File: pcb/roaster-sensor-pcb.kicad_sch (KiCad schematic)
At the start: 3 parts, among them U1 Pico

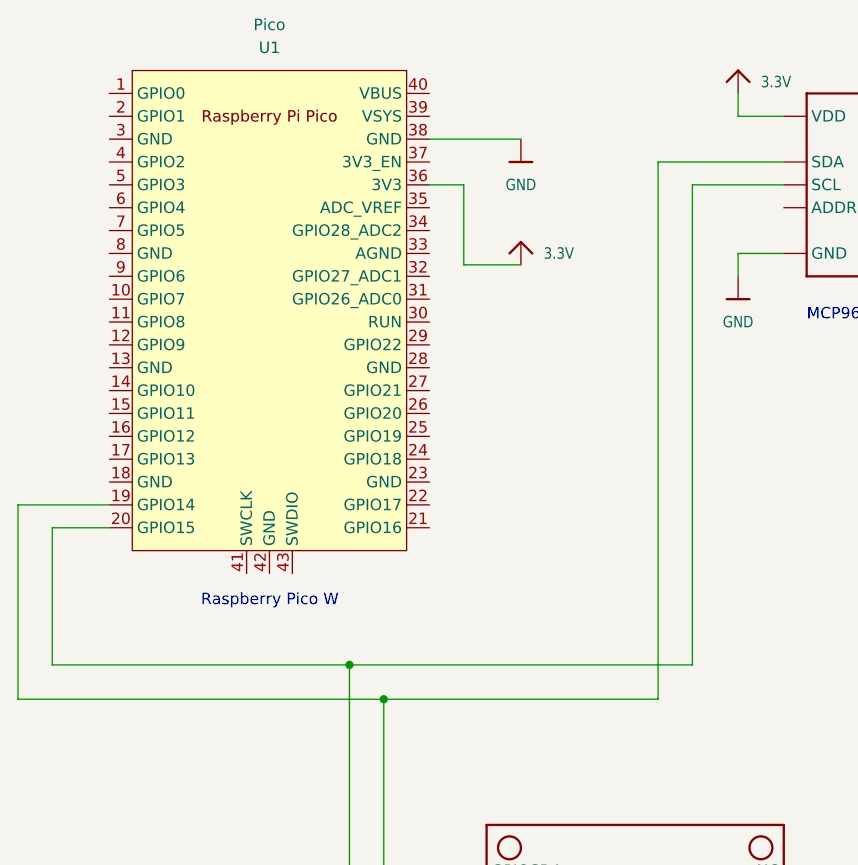
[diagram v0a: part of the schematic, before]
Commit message: changed pinout and disable display for perf proto
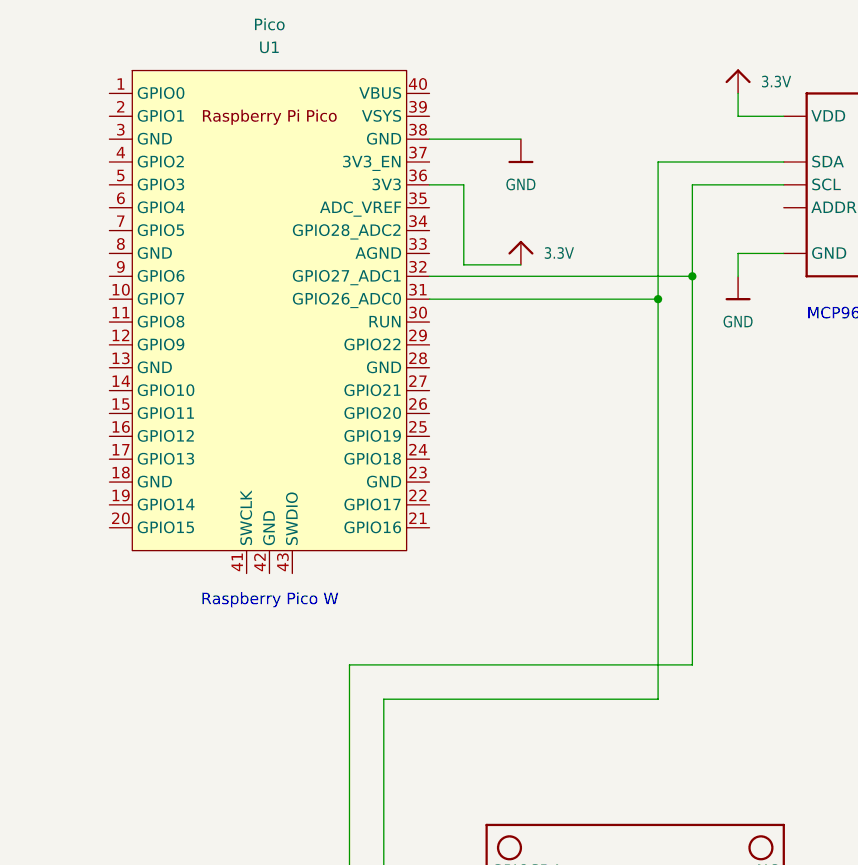
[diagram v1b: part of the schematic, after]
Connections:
- net at MS1.17 (GPIOSDA), MS1.17B (GPIOSDA), U2.20 (SDA): now also U1.31 (GPIO26_ADC0); no longer U1.19 (GPIO14)
- net at MS1.18 (GPIOSCL), MS1.18B (GPIOSCL), U2.19 (SCL): now also U1.32 (GPIO27_ADC1); no longer U1.20 (GPIO15)
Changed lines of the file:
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@@
 (kicad_sch (version 20230121) (generator eeschema)
   (paper "A4")
-  (junction (at 90.17 102.87) (diameter 0) (color 0 0 0 0)
-  )
-  (junction (at 86.36 99.06) (diameter 0) (color 0 0 0 0)
+  (junction (at 120.65 58.42) (diameter 0) (color 0 0 0 0)
   )
   (junction (at 148.59 157.48) (diameter 0) (color 0 0 0 0)
+  )
+  (junction (at 124.46 55.88) (diameter 0) (color 0 0 0 0)
   )
   (wire (pts (xy 90.17 102.87) (xy 120.65 102.87))
@@
   )
   (wire (pts (xy 90.17 121.92) (xy 96.52 121.92))
-    (stroke (width 0) (type default))
-  )
-  (wire (pts (xy 59.69 81.28) (xy 49.53 81.28))
     (stroke (width 0) (type default))
   )
@@
     (stroke (width 0) (type default))
   )
-  (wire (pts (xy 53.34 83.82) (xy 53.34 99.06))
-    (stroke (width 0) (type default))
-  )
   (wire (pts (xy 129.54 55.88) (xy 129.54 53.34))
     (stroke (width 0) (type default))
@@
     (stroke (width 0) (type default))
   )
-  (wire (pts (xy 49.53 102.87) (xy 90.17 102.87))
-    (stroke (width 0) (type default))
-  )
   (wire (pts (xy 95.25 40.64) (xy 105.41 40.64))
     (stroke (width 0) (type default))
   )
-  (wire (pts (xy 120.65 43.18) (xy 120.65 102.87))
+  (wire (pts (xy 120.65 43.18) (xy 120.65 58.42))
     (stroke (width 0) (type default))
   )
@@
     (stroke (width 0) (type default))
   )
-  (wire (pts (xy 124.46 99.06) (xy 124.46 45.72))
+  (wire (pts (xy 124.46 99.06) (xy 124.46 55.88))
     (stroke (width 0) (type default))
   )
@@
     (stroke (width 0) (type default))
   )
+  (wire (pts (xy 124.46 55.88) (xy 124.46 45.72))
+    (stroke (width 0) (type default))
+  )
   (wire (pts (xy 143.51 152.4) (xy 139.7 152.4))
     (stroke (width 0) (type default))
@@
     (stroke (width 0) (type default))
   )
-  (wire (pts (xy 59.69 83.82) (xy 53.34 83.82))
-    (stroke (width 0) (type default))
-  )
   (wire (pts (xy 139.7 157.48) (xy 148.59 157.48))
     (stroke (width 0) (type default))
@@
     (stroke (width 0) (type default))
   )
+  (wire (pts (xy 120.65 58.42) (xy 120.65 102.87))
+    (stroke (width 0) (type default))
+  )
   (wire (pts (xy 148.59 147.32) (xy 143.51 147.32))
     (stroke (width 0) (type default))
   )
-  (wire (pts (xy 49.53 81.28) (xy 49.53 102.87))
+  (wire (pts (xy 95.25 55.88) (xy 124.46 55.88))
     (stroke (width 0) (type default))
   )
-  (wire (pts (xy 53.34 99.06) (xy 86.36 99.06))
+  (wire (pts (xy 95.25 58.42) (xy 120.65 58.42))
     (stroke (width 0) (type default))
   )
